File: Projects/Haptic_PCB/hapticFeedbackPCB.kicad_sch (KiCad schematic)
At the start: 16 parts, among them M1 Motor_DC, M2 Motor_DC, M3 Motor_DC, Q1 NPN, Q2 NPN, Q3 NPN

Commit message: Added some footprints
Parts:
- D1, D2, D3: footprint (none) -> Diode_THT:D_5W_P10.16mm_Horizontal
- R1, R2, R3: footprint (none) -> Resistor_THT:R_Axial_DIN0207_L6.3mm_D2.5mm_P10.16mm_Horizontal
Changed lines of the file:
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@@
 			)
 		)
-		(property "Footprint" ""
+		(property "Footprint" "Diode_THT:D_5W_P10.16mm_Horizontal"
 			(at 109.22 52.07 0)
 			(effects
@@
 			)
 		)
-		(property "Footprint" ""
+		(property "Footprint" "Resistor_THT:R_Axial_DIN0207_L6.3mm_D2.5mm_P10.16mm_Horizontal"
 			(at 90.17 131.318 90)
 			(effects
@@
 			)
 		)
-		(property "Footprint" ""
+		(property "Footprint" "Resistor_THT:R_Axial_DIN0207_L6.3mm_D2.5mm_P10.16mm_Horizontal"
 			(at 90.17 95.758 90)
 			(effects
@@
 			)
 		)
-		(property "Footprint" ""
+		(property "Footprint" "Diode_THT:D_5W_P10.16mm_Horizontal"
 			(at 110.49 85.09 0)
 			(effects
@@
 			)
 		)
-		(property "Footprint" ""
+		(property "Footprint" "Resistor_THT:R_Axial_DIN0207_L6.3mm_D2.5mm_P10.16mm_Horizontal"
 			(at 90.17 62.738 90)
 			(effects
@@
 			)
 		)
-		(property "Footprint" ""
+		(property "Footprint" "Diode_THT:D_5W_P10.16mm_Horizontal"
 			(at 110.49 120.65 0)
 			(effects

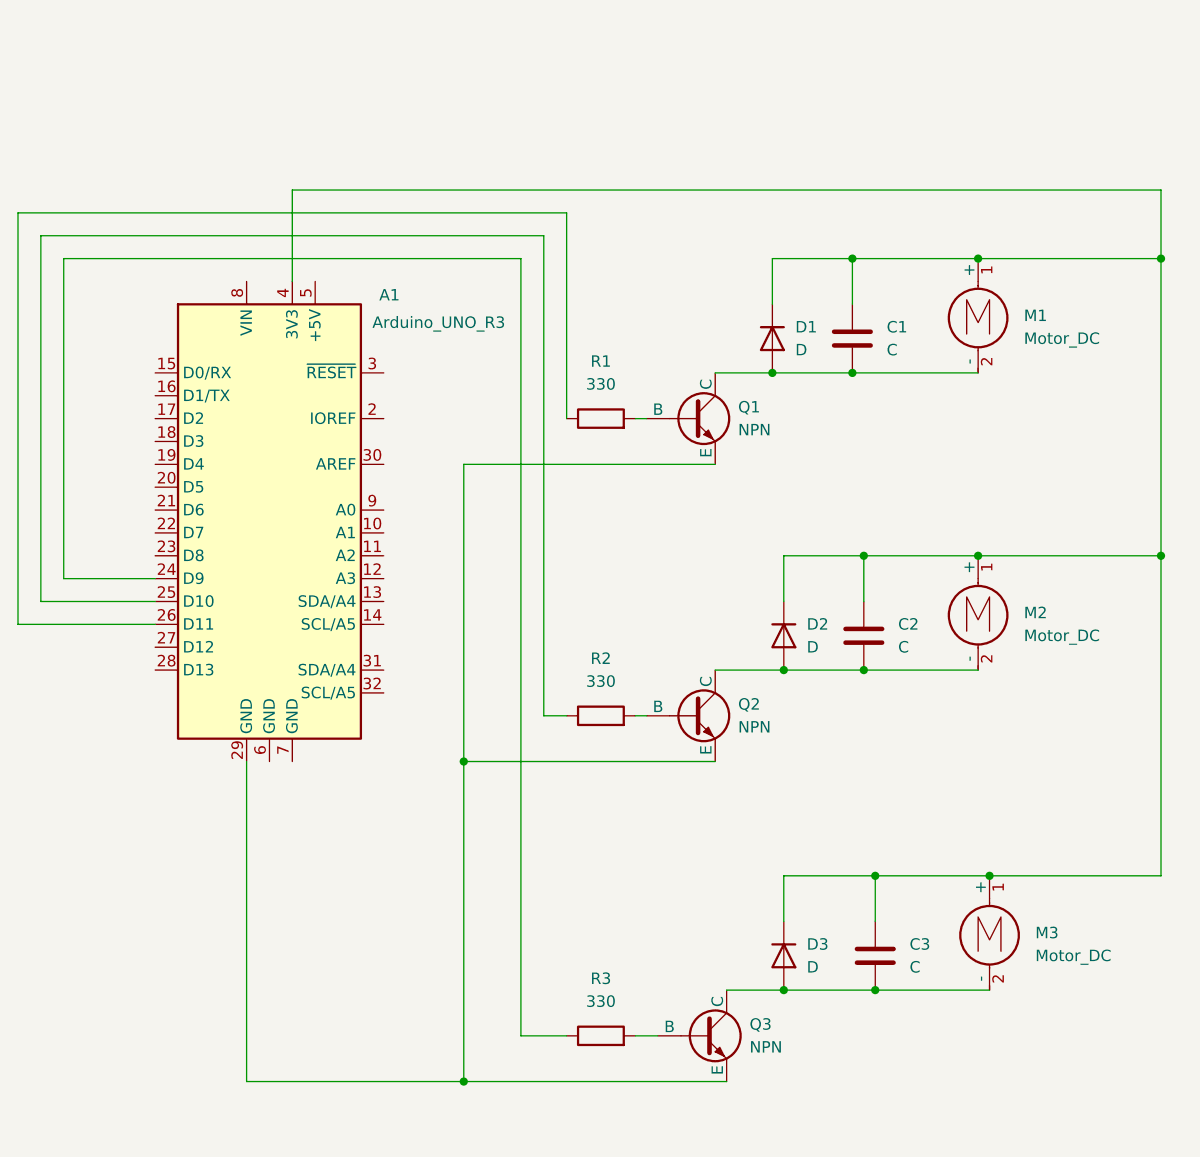
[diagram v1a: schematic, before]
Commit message: Added all footprints
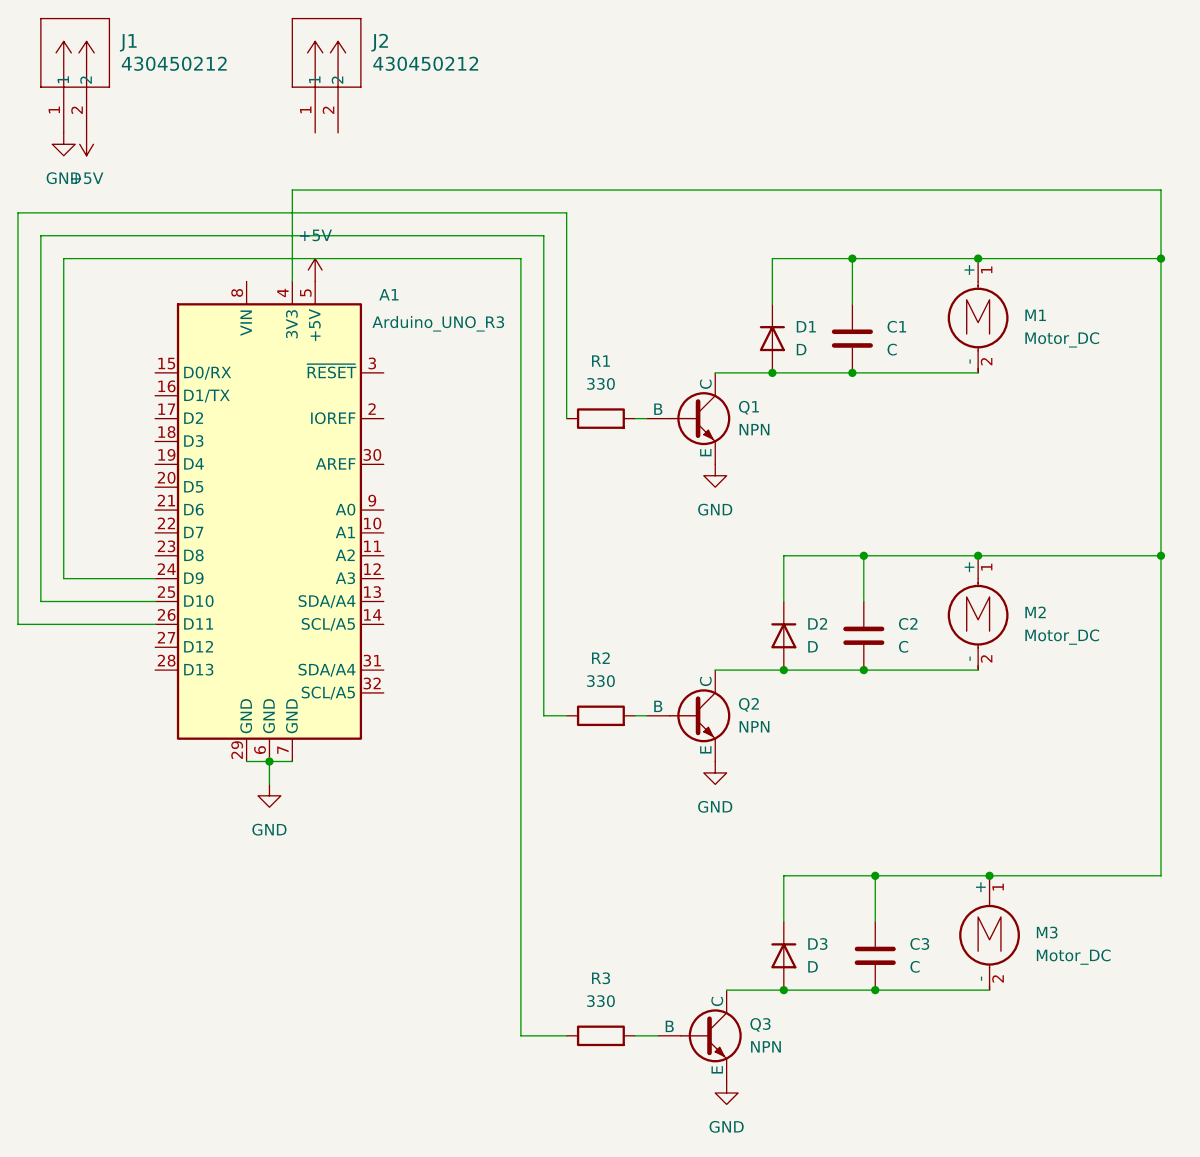
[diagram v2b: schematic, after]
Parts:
- added J1, J2: 430450212, Molex 2 x 1:CON_430450212_MOL, symbol Molex 2 x 1:430450212
- C1, C2, C3: footprint (none) -> Capacitor_THT:CP_Radial_D8.0mm_P5.00mm
- M1, M2, M3: footprint (none) -> Molex 2 x 1:CON_430450212_MOL
- Q1, Q2, Q3: footprint (none) -> NPN:TO-18_TO-206AA_5P8_ONS
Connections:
- net GND: now reaches A1.29 (GND), Q1.3 (E), Q2.3 (E), Q3.3 (E)
- net GND: now also A1.6 (GND), A1.7 (GND), J1.1
- net +5V: now reaches A1.5 (+5V)
- net +5V: now also J1.2

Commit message: Created preliminary PCB layout
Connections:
- net +5V: now also C1.1, C2.1, C3.1, D1.1 (K), D2.1 (K), D3.1 (K), M1.1 (+), M2.1 (+), M3.1 (+)
- now unconnected: A1.4 (3V3)
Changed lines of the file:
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@@
+	)
+	(junction
+		(at 152.4 43.18)
+		(diameter 0)
+		(color 0 0 0 0)
 	)
 	(junction
@@
 	)
 	(junction
-		(at 152.4 43.18)
-		(diameter 0)
-		(color 0 0 0 0)
-	)
-	(junction
 		(at 110.49 124.46)
 		(diameter 0)
@@
 	(wire
 		(pts
-			(xy 152.4 35.56) (xy 152.4 43.18)
-		)
-		(stroke
-			(width 0)
-			(type default)
-		)
-	)
-	(wire
-		(pts
 			(xy 118.11 43.18) (xy 118.11 48.26)
 		)
@@
 	(wire
 		(pts
-			(xy 55.88 45.72) (xy 55.88 35.56)
-		)
-		(stroke
-			(width 0)
-			(type default)
-		)
-	)
-	(wire
-		(pts
 			(xy 81.28 129.54) (xy 81.28 43.18)
 		)
@@
 		(pts
 			(xy 25.4 83.82) (xy 40.64 83.82)
-		)
-		(stroke
-			(width 0)
-			(type default)
-		)
-	)
-	(wire
-		(pts
-			(xy 55.88 35.56) (xy 152.4 35.56)
 		)
 		(stroke
@@
 					(unit 1)
 				)
+			)
+		)
+	)
+	(symbol
+		(lib_id "power:+5V")
+		(at 152.4 43.18 0)
+		(unit 1)
+		(exclude_from_sim no)
+		(in_bom yes)
+		(on_board yes)
+		(dnp no)
+		(fields_autoplaced yes)
+		(property "Reference" "#PWR08"
+			(at 152.4 46.99 0)
+			(effects
+				(font
+					(size 1.27 1.27)
+				)
+				(hide yes)
+			)
+		)
+		(property "Value" "+5V"
+			(at 152.4 38.1 0)
+			(effects
+				(font
+					(size 1.27 1.27)
+				)
+			)
+		)
+		(property "Footprint" ""
+			(at 152.4 43.18 0)
+			(effects
+				(font
+					(size 1.27 1.27)
+				)
+				(hide yes)
+			)
+		)
+		(property "Datasheet" ""
+			(at 152.4 43.18 0)
+			(effects
+				(font
+					(size 1.27 1.27)
+				)
+				(hide yes)
+			)
+		)
+		(property "Description" "Power symbol creates a global label with name \"+5V\""
+			(at 152.4 43.18 0)
+			(effects
+				(font
+					(size 1.27 1.27)
+				)
+				(hide yes)
+			)
+		)
+		(pin "1"
+		)
+		(instances
+			(project "hapticFeedbackPCB"
+				(path "/8672886c-60c5-432f-932f-9e8bb677a199"
+					(reference "#PWR08")
+					(unit 1)
+				)
